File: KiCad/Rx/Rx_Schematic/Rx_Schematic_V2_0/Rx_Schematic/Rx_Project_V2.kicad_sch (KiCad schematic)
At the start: 9 parts, among them J1 Conn_01x05, J2 Conn_01x02, J3 Conn_01x06, J4 Conn_01x02, U1 ProMicro

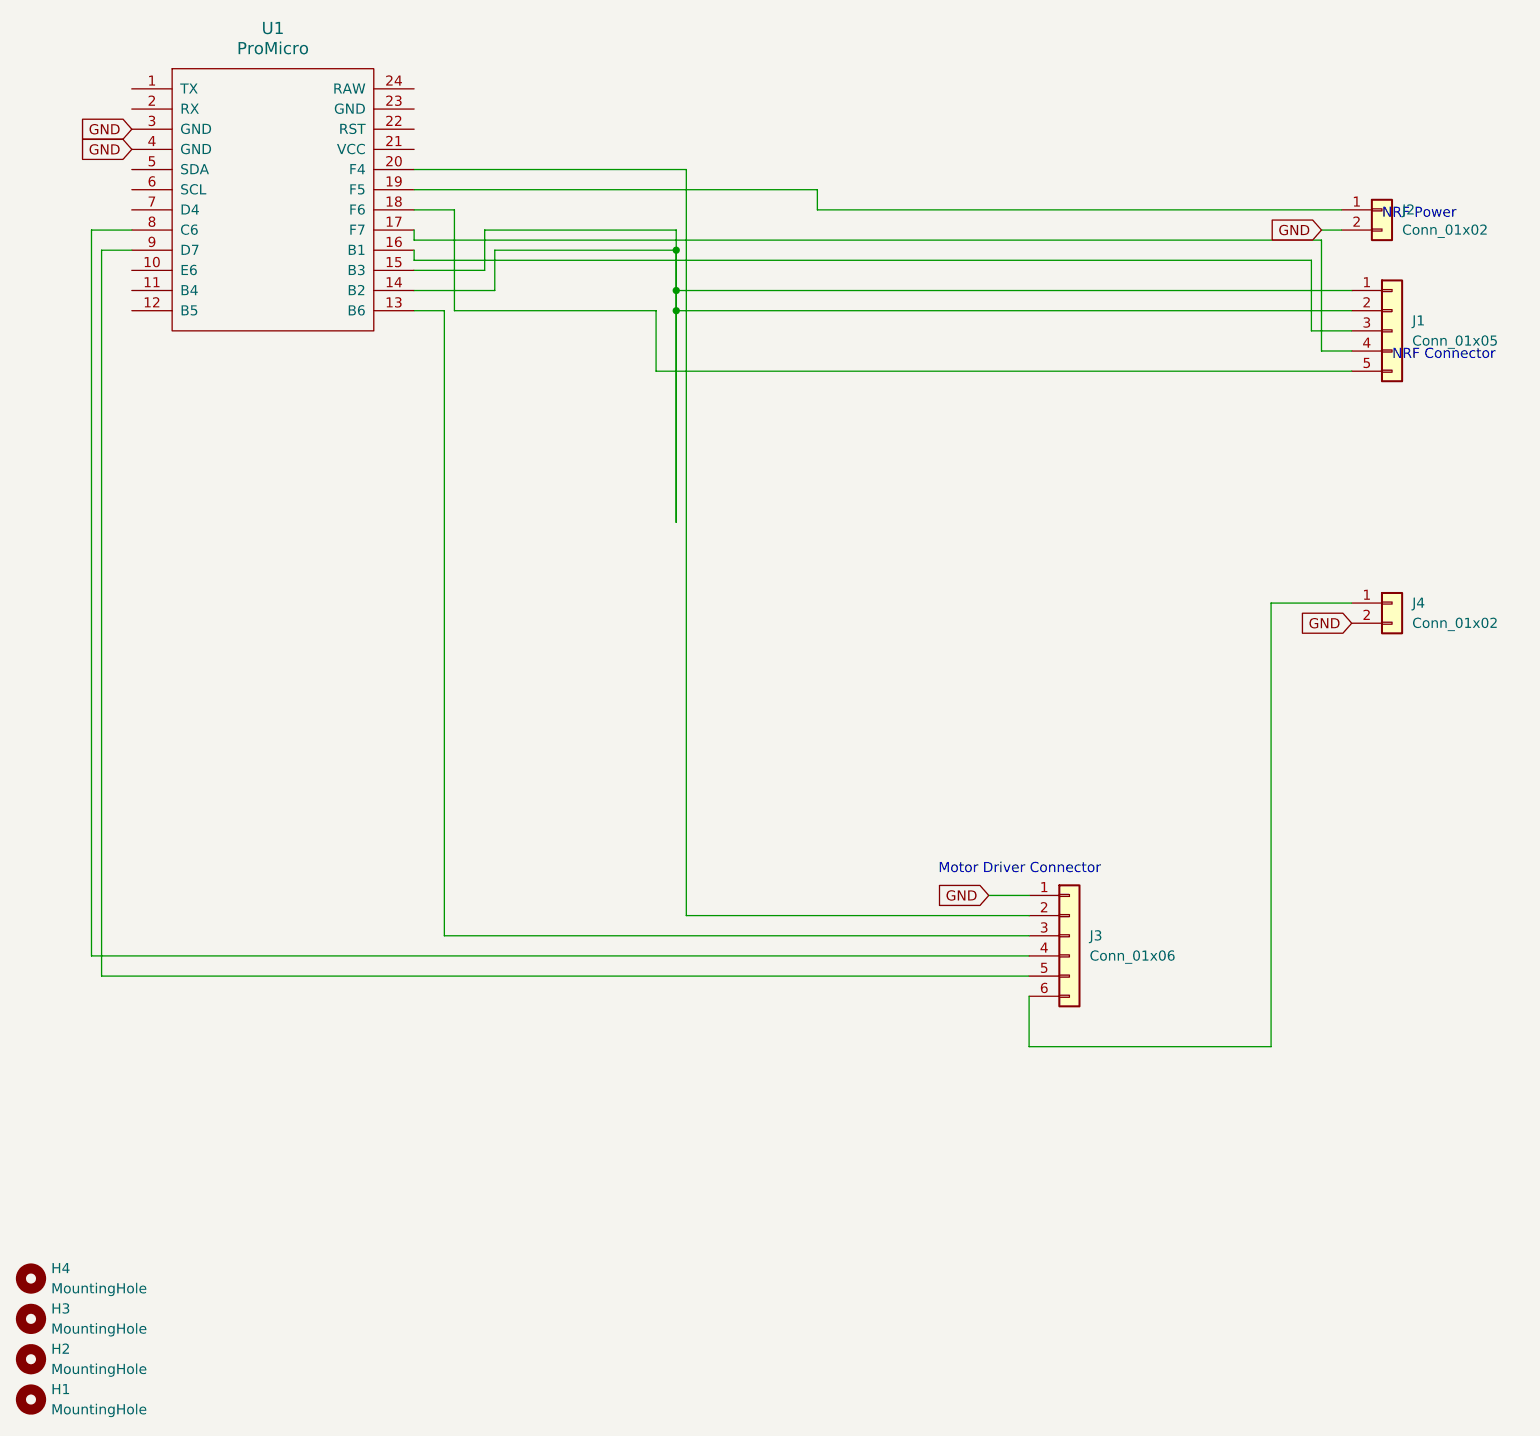
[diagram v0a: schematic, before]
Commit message: Remade file to remove nano and add connector pins in place
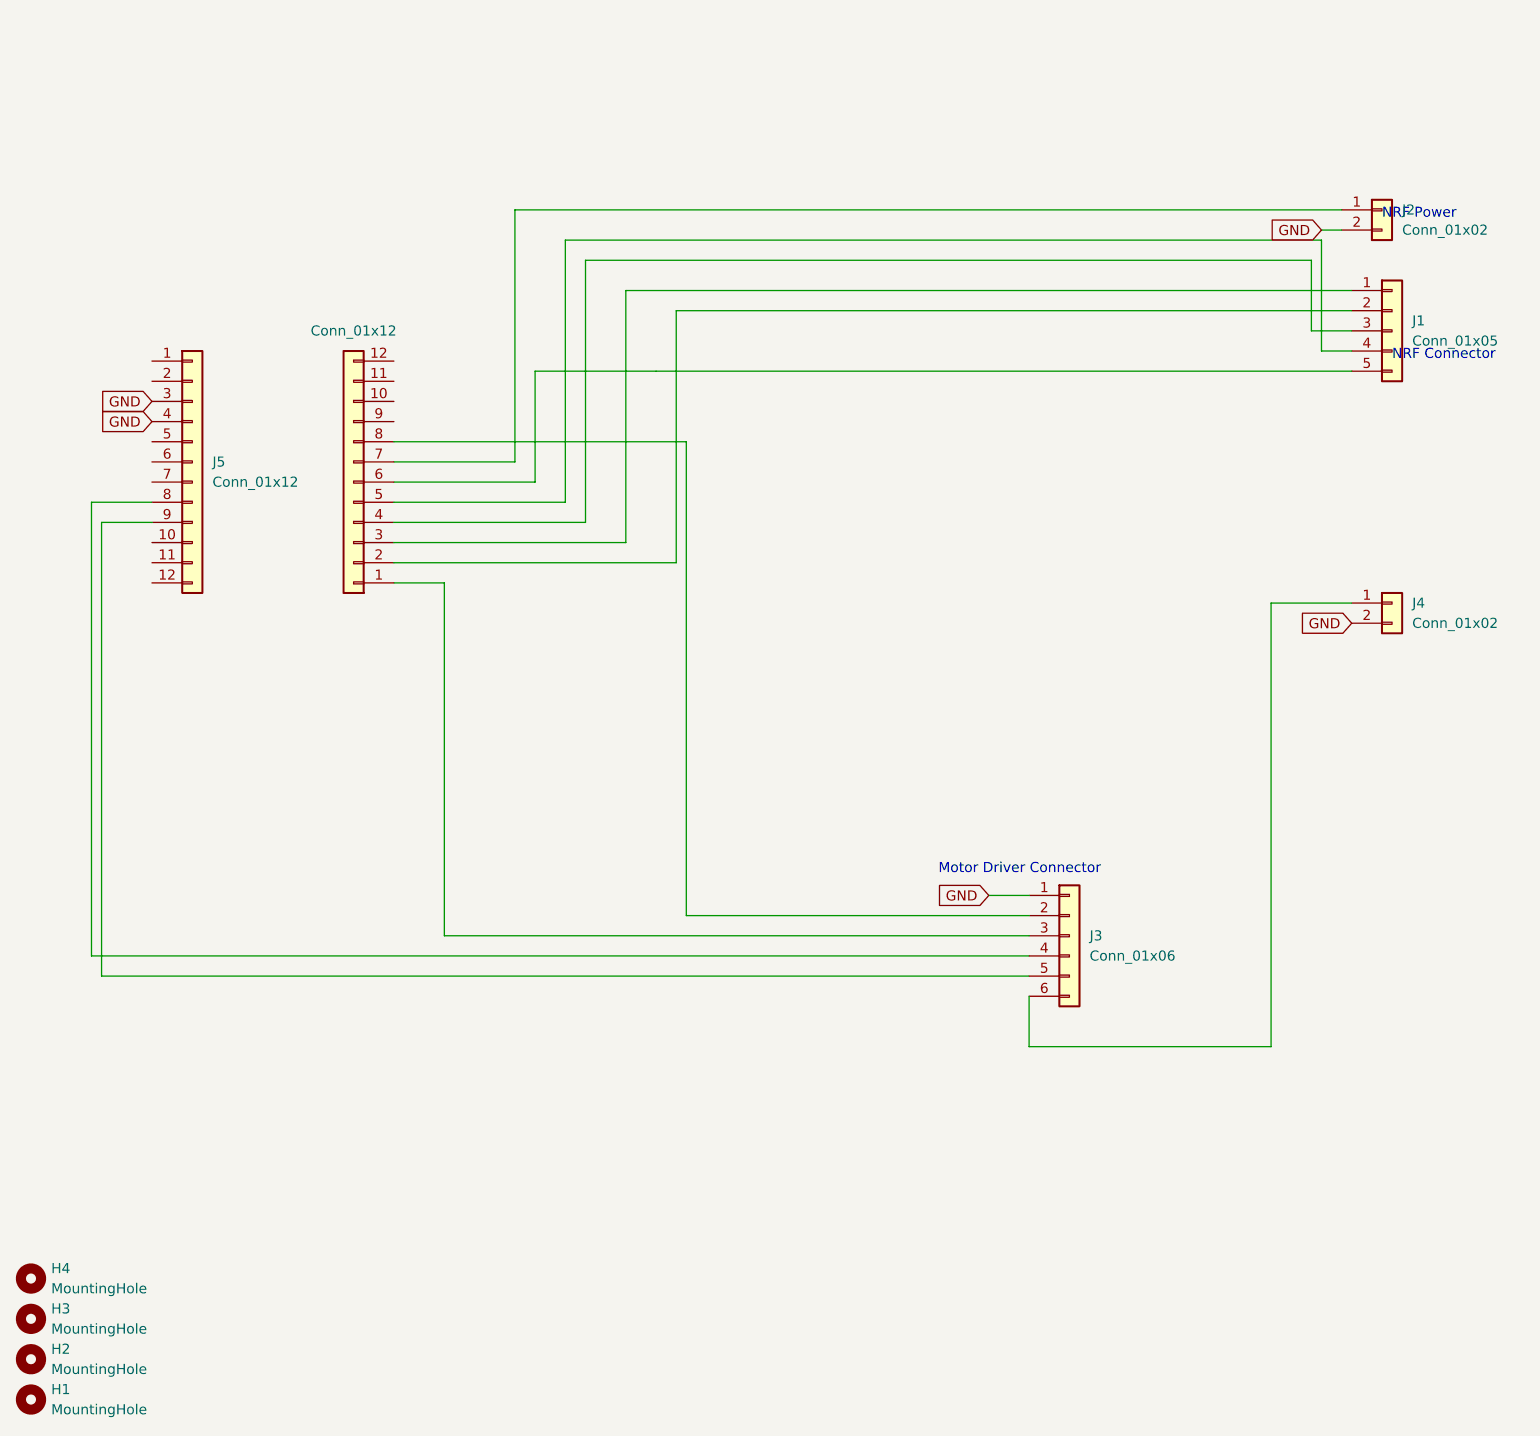
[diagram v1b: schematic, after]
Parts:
- removed U1: ProMicro, promicro:ProMicro, symbol promicro:ProMicro
- added J5, J6: Conn_01x12, Connector_PinSocket_2.54mm:PinSocket_1x12_P2.54mm_Vertical, symbol Connector_Generic:Conn_01x12
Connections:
- net GND: now also J5.3 (Pin_3), J5.4 (Pin_4)
- net at J3.3 (Pin_3): now also J6.1 (Pin_1)
- net at J1.2 (Pin_2): now also J6.2 (Pin_2); no longer J1.1 (Pin_1)
- net at J1.3 (Pin_3): now also J6.4 (Pin_4)
- net at J1.4 (Pin_4): now also J6.5 (Pin_5)
- net at J1.5 (Pin_5): now also J6.6 (Pin_6)
- net at J2.1 (Pin_1): now also J6.7 (Pin_7)
- net at J3.2 (Pin_2): now also J6.8 (Pin_8)
- net at J3.4 (Pin_4): now also J5.8 (Pin_8)
- net at J3.5 (Pin_5): now also J5.9 (Pin_9)
- new net: J1.1 (Pin_1), J6.3 (Pin_3)
